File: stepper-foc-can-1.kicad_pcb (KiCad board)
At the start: 4 copper layers, 42 x 48 mm, 87 parts, among them J1 TC2030, J2 Conn_01x02, J3 Conn_01x04_Pin, J4 Conn_01x02, J5 Conn_01x02, M1 Stepper_Motor_bipolar, SW1 SW_Push, SW2 SW_Push, SW3 SW_Push, SW4 SW_Push, U1 STM32G474RBTx, U2 MX25947, U3 TPS62933, U4 TCAN3413, U5 AS5047P, U6 DRV8874, U7 INA241A3IDDF, U8 DRV8874, U9 INA241A3IDDF, Y1 Crystal_GND24

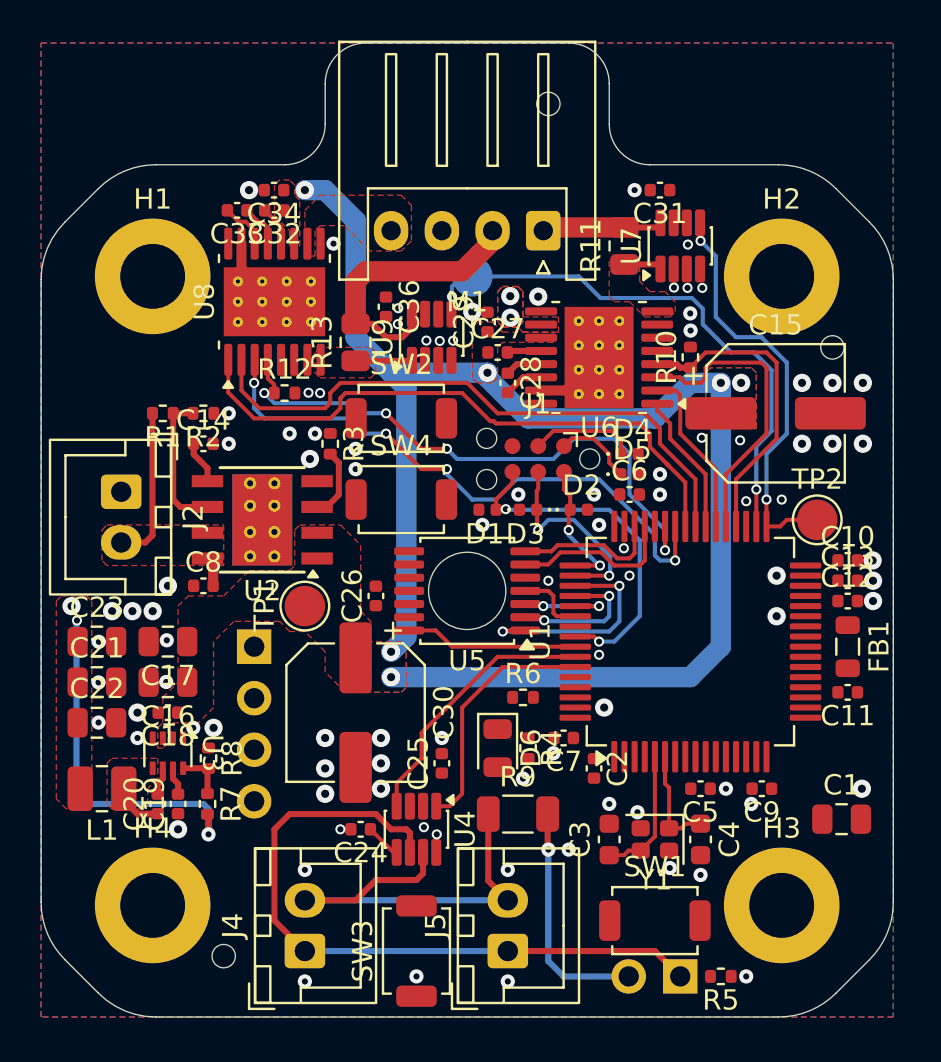
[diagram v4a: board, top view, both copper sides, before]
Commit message: pcb: add +3v3 pwr routing
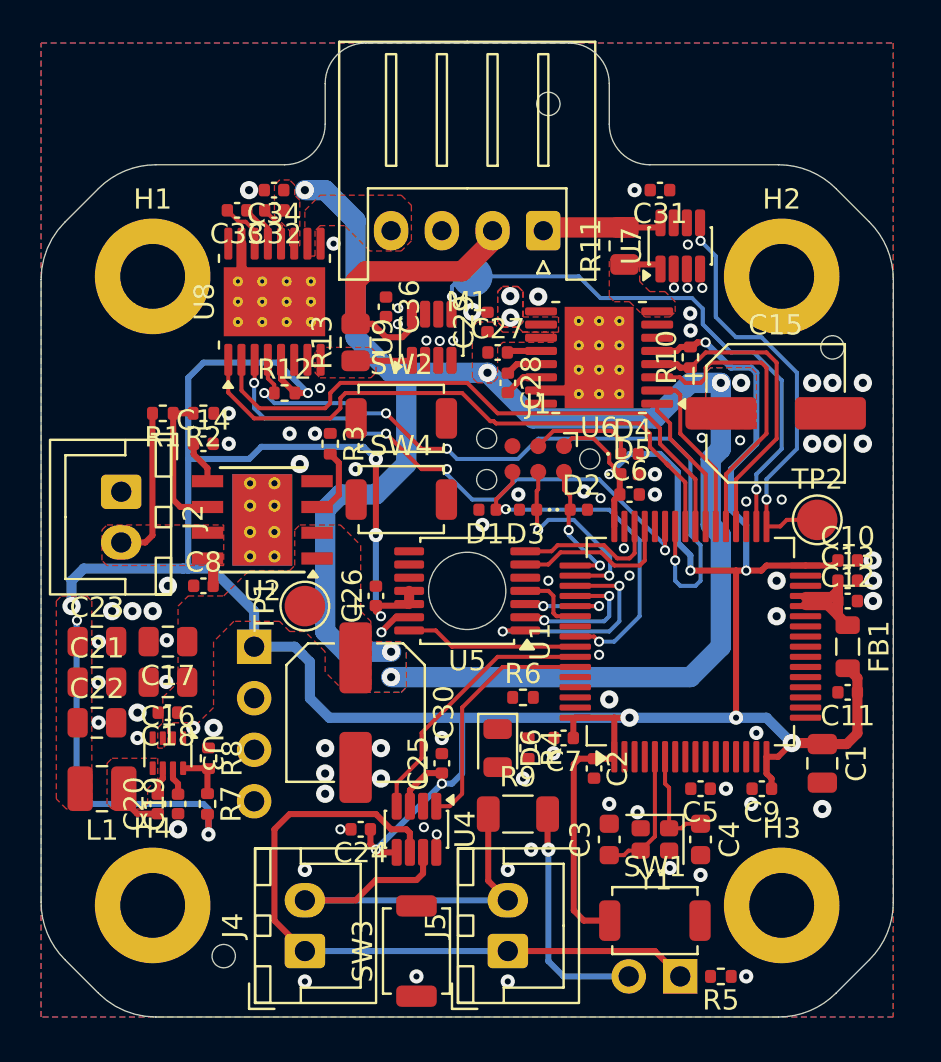
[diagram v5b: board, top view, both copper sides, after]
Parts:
- moved C1 2.91 mm to (161.5, 89.5), turned to -90 degrees
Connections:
- U1 pad 42: /~{SLEEP_B} -> /~{FAULT_B}
- U1 pad 43: /~{FAULT_B} -> /~{SLEEP_B}
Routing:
- net +3V3: track 23.2 -> 187.8 mm, vias 3 -> 16
- net /~{FAULT_B}: track 29.0 -> 35.8 mm
- net +VDDA: track 0.00 -> 5.91 mm
- net +12V: track 73.6 -> 78.6 mm
- net GND: track 7.07 -> 8.76 mm, vias 91 -> 90
- net /~{SLEEP_B}: track 29.5 -> 27.8 mm

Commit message: pcb: route vref
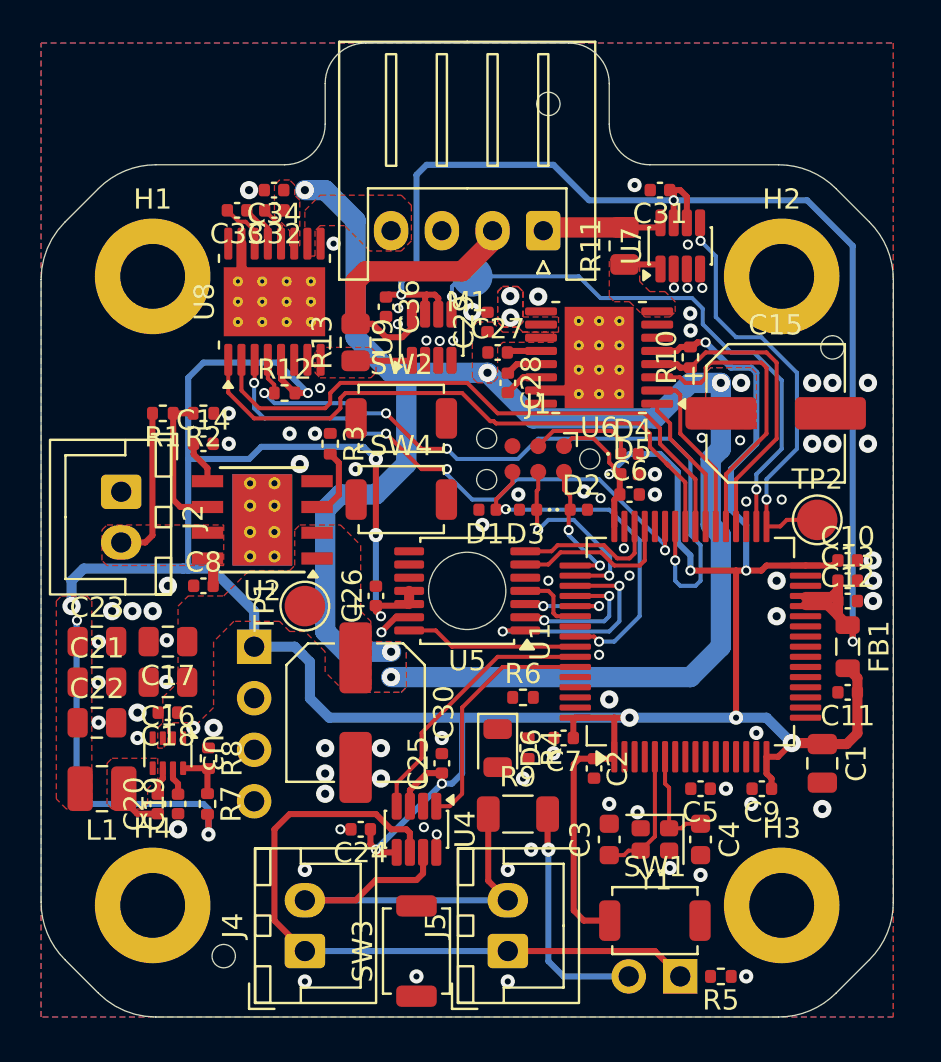
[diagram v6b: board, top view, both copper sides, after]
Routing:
- net +VDDA: track 5.91 -> 64.3 mm, vias 0 -> 3
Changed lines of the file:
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@@
 	)
 	(via
-		(at 163.5 70.75)
+		(at 163.75 70.75)
 		(size 0.9)
 		(drill 0.4)
@@
 	)
 	(via
-		(at 163.5 73.75)
+		(at 163.75 73.75)
 		(size 0.9)
 		(drill 0.4)
@@
 	)
 	(via
-		(at 152.25 61.25)
+		(at 152.25 61)
 		(size 0.7)
 		(drill 0.3)
@@
 	)
 	(segment
+		(start 154.175 61.445)
+		(end 153.98 61.25)
+		(width 0.3)
+		(layer "F.Cu")
+		(net "+VDDA")
+	)
+	(segment
 		(start 162.27 81.5)
 		(end 162.27 81)
@@
 	)
 	(segment
+		(start 142.575 66.575)
+		(end 142.575 67.3625)
+		(width 0.3)
+		(layer "F.Cu")
+		(net "+VDDA")
+	)
+	(segment
+		(start 163 83.5)
+		(end 163 82.9375)
+		(width 0.3)
+		(layer "F.Cu")
+		(net "+VDDA")
+	)
+	(segment
+		(start 141.925 67.3625)
+		(end 141.925 66.475)
+		(width 0.3)
+		(layer "F.Cu")
+		(net "+VDDA")
+	)
+	(segment
+		(start 154.175 62.8625)
+		(end 154.175 61.445)
+		(width 0.3)
+		(layer "F.Cu")
+		(net "+VDDA")
+	)
+	(segment
+		(start 142 66.4)
+		(end 142.4 66.4)
+		(width 0.3)
+		(layer "F.Cu")
+		(net "+VDDA")
+	)
+	(segment
+		(start 140.12 66.4)
+		(end 140.75 66.4)
+		(width 0.3)
+		(layer "F.Cu")
+		(net "+VDDA")
+	)
+	(segment
+		(start 154.825 61.575)
+		(end 154.5 61.25)
+		(width 0.3)
+		(layer "F.Cu")
+		(net "+VDDA")
+	)
+	(segment
 		(start 162.27 81)
 		(end 162.27 80.5)
@@
 	)
 	(segment
+		(start 141.925 66.475)
+		(end 142 66.4)
+		(width 0.3)
+		(layer "F.Cu")
+		(net "+VDDA")
+	)
+	(segment
+		(start 140 66.52)
+		(end 140.12 66.4)
+		(width 0.3)
+		(layer "F.Cu")
+		(net "+VDDA")
+	)
+	(segment
 		(start 162.27 81)
 		(end 161.97 81.3)
@@
 	)
 	(segment
+		(start 154.5 61.25)
+		(end 153.98 61.25)
+		(width 0.3)
+		(layer "F.Cu")
+		(net "+VDDA")
+	)
+	(segment
 		(start 161.97 81.3)
 		(end 160.675 81.3)
@@
 	)
 	(segment
+		(start 154.825 62.8625)
+		(end 154.825 61.575)
+		(width 0.3)
+		(layer "F.Cu")
+		(net "+VDDA")
+	)
+	(segment
+		(start 142.4 66.4)
+		(end 142.575 66.575)
+		(width 0.3)
+		(layer "F.Cu")
+		(net "+VDDA")
+	)
+	(segment
+		(start 163 82.9375)
+		(end 162.75 82.6875)
+		(width 0.3)
+		(layer "F.Cu")
+		(net "+VDDA")
+	)
+	(segment
+		(start 140.75 66.4)
+		(end 142 66.4)
+		(width 0.3)
+		(layer "F.Cu")
+		(net "+VDDA")
+	)
+	(segment
 		(start 162.75 82.6875)
 		(end 162.27 82.2075)
@@
 		(net "+VDDA")
 	)
+	(via
+		(at 140.75 66.4)
+		(size 0.5)
+		(drill 0.3)
+		(layers "F.Cu" "B.Cu")
+		(net "+VDDA")
+	)
+	(via
+		(at 163 83.5)
+		(size 0.5)
+		(drill 0.3)
+		(layers "F.Cu" "B.Cu")
+		(net "+VDDA")
+	)
+	(via
+		(at 154.175 61.75)
+		(size 0.5)
+		(drill 0.3)
+		(layers "F.Cu" "B.Cu")
+		(net "+VDDA")
+	)
+	(segment
+		(start 141.5 65)
+		(end 140.75 65.75)
+		(width 0.3)
+		(layer "B.Cu")
+		(net "+VDDA")
+	)
+	(segment
+		(start 163 83.5)
+		(end 163 64)
+		(width 0.3)
+		(layer "B.Cu")
+		(net "+VDDA")
+	)
+	(segment
+		(start 163 64)
+		(end 160.75 61.75)
+		(width 0.3)
+		(layer "B.Cu")
+		(net "+VDDA")
+	)
+	(segment
+		(start 154.175 61.75)
+		(end 150 61.75)
+		(width 0.3)
+		(layer "B.Cu")
+		(net "+VDDA")
+	)
+	(segment
+		(start 140.75 65.75)
+		(end 140.75 66.4)
+		(width 0.3)
+		(layer "B.Cu")
+		(net "+VDDA")
+	)
+	(segment
+		(start 148.25 60)
+		(end 142 60)
+		(width 0.3)
+		(layer "B.Cu")
+		(net "+VDDA")
+	)
+	(segment
+		(start 160.75 61.75)
+		(end 154.175 61.75)
+		(width 0.3)
+		(layer "B.Cu")
+		(net "+VDDA")
+	)
+	(segment
+		(start 150 61.75)
+		(end 148.25 60)
+		(width 0.3)
+		(layer "B.Cu")
+		(net "+VDDA")
+	)
+	(segment
+		(start 142 60)
+		(end 141.5 60.5)
+		(width 0.3)
+		(layer "B.Cu")
+		(net "+VDDA")
+	)
+	(segment
+		(start 141.5 60.5)
+		(end 141.5 65)
+		(width 0.3)
+		(layer "B.Cu")
+		(net "+VDDA")
+	)

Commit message: pcb: route nrst
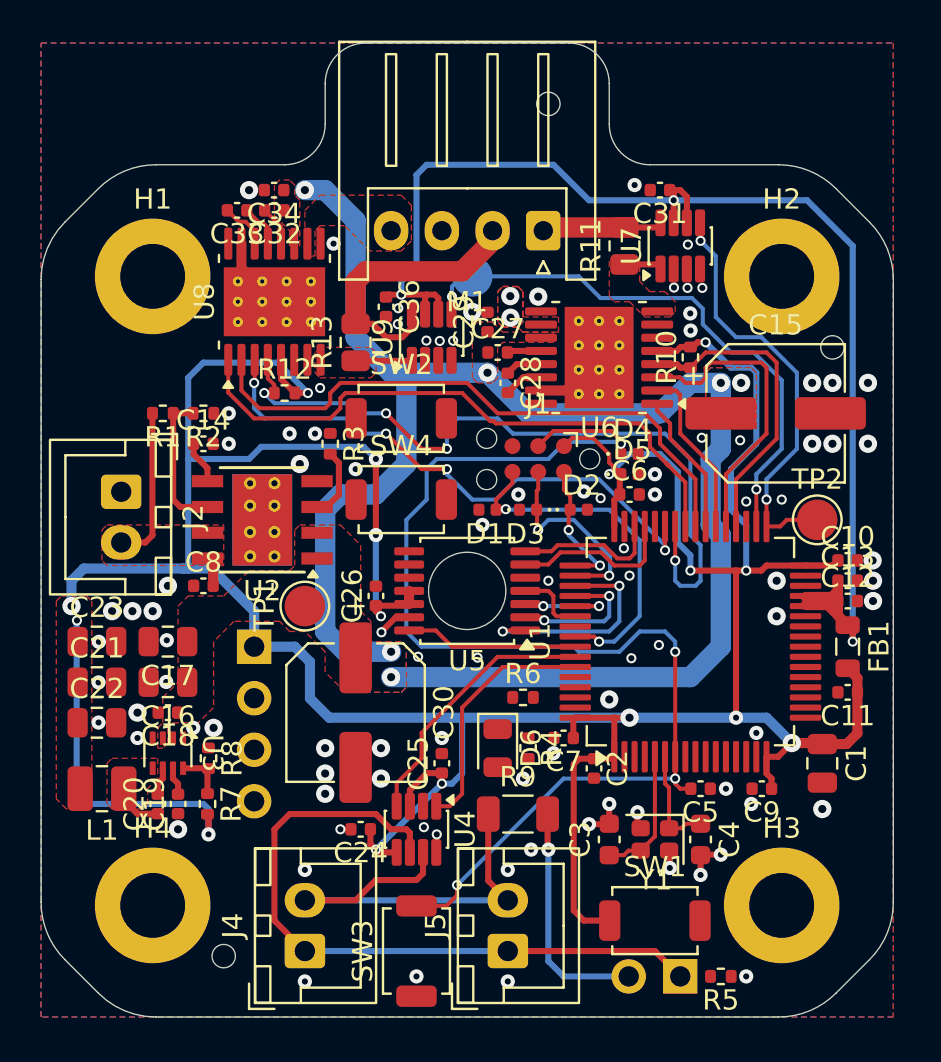
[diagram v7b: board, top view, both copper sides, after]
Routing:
- net /NRST: track 5.25 -> 61.6 mm, vias 0 -> 4
- net GND: track 8.76 -> 14.5 mm, vias 90 -> 95
- net /~{FAULT_B}: track 35.8 -> 36.8 mm

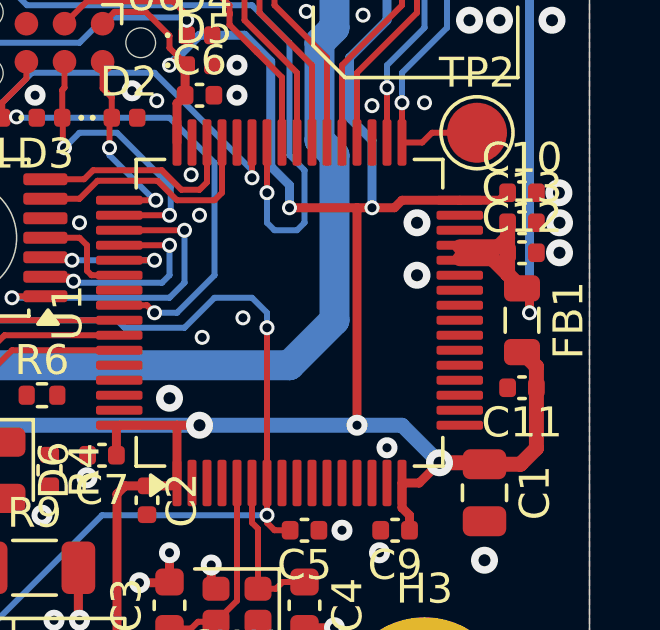
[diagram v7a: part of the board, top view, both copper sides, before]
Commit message: pcb: route id jumpers
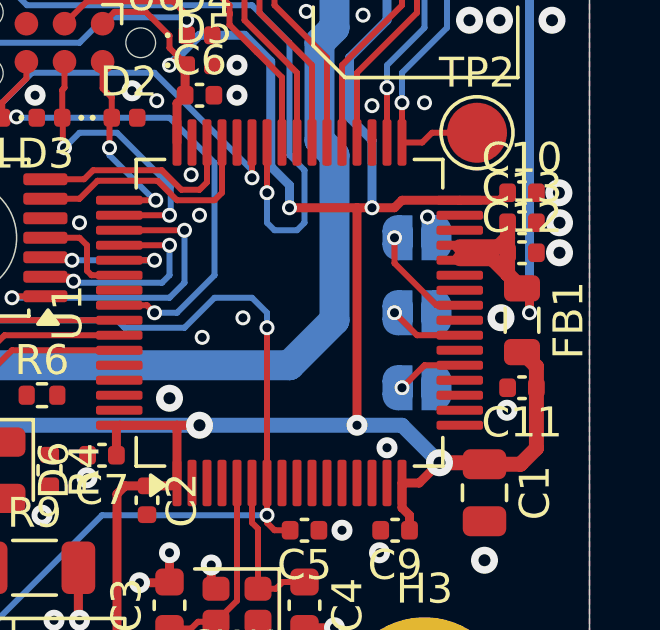
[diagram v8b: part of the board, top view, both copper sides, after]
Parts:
- added JP2: Jumper_2_Open, Jumper:SolderJumper-2_P1.3mm_Open_RoundedPad1.0x1.5mm, B.Cu at (159.2, 86.0)
- added JP3: Jumper_2_Open, Jumper:SolderJumper-2_P1.3mm_Open_RoundedPad1.0x1.5mm, B.Cu at (159.2, 83.5)
- added JP4: Jumper_2_Open, Jumper:SolderJumper-2_P1.3mm_Open_RoundedPad1.0x1.5mm, B.Cu at (159.2, 81.0)
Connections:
- U1 pad 21: unconnected-(U1-PA7-Pad21) -> /ID_1
- U1 pad 23: unconnected-(U1-PC5-Pad23) -> /ID_2
- U1 pad 25: unconnected-(U1-PB1-Pad25) -> /ID_3
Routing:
- net /ID_3: track 0.00 -> 3.60 mm, vias 0 -> 1
- net /ID_2: track 0.00 -> 2.49 mm, vias 0 -> 1
- net /ID_1: track 0.00 -> 2.24 mm, vias 0 -> 1
- net GND: vias 95 -> 96
